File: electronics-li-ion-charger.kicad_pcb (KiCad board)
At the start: 2 copper layers, 19.1 x 25.4 mm, 20 parts, among them J1 Conn_01x01_Male, J2 Conn_01x01_Male, J3 USB_B_Micro, J4 Conn_01x03_Male, U1 MCP73831-2-OT

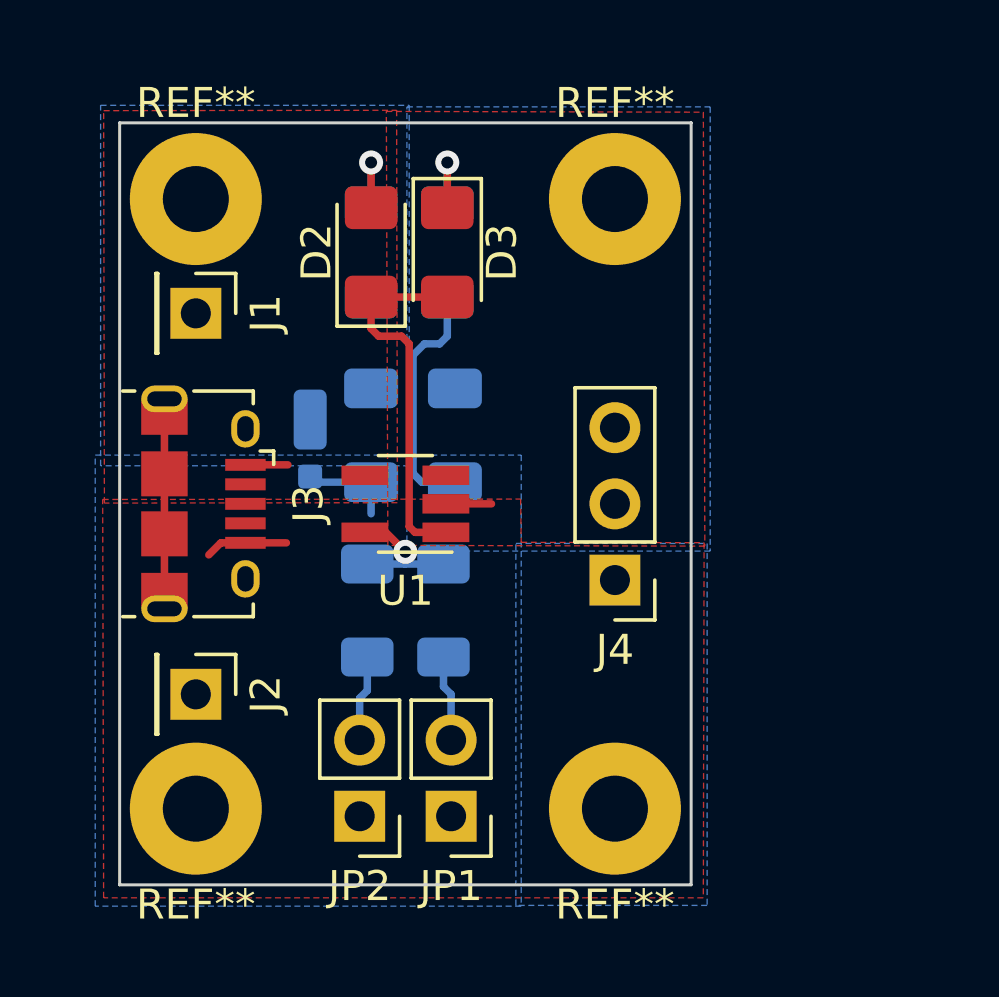
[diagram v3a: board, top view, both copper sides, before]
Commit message: Add silkscreen text.
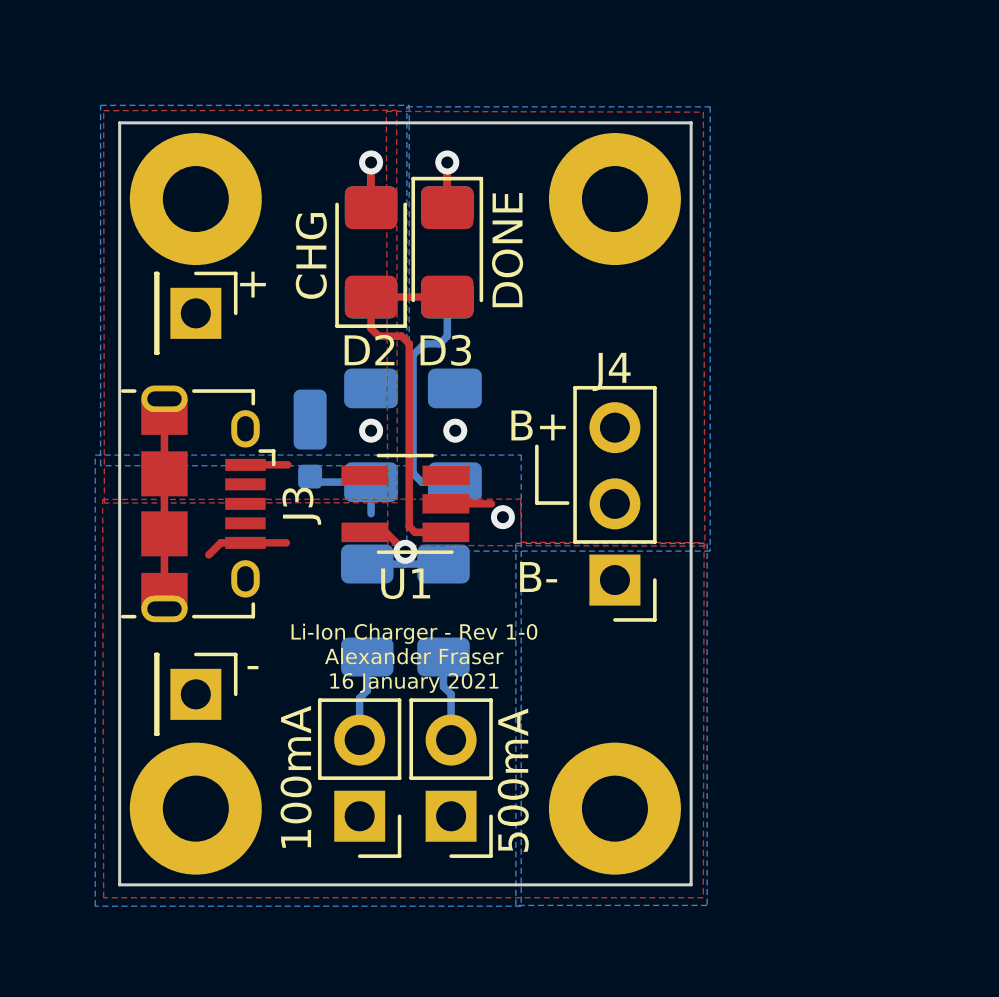
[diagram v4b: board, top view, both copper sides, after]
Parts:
- renumbered REF** to M1, REF** to M2, REF** to M3, REF** to M4
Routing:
- net GND: vias 0 -> 1
- net /VBAT: vias 0 -> 1
- net +5V: vias 0 -> 1
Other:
- board text added: "+"
- board text added: "-"
- board text added: "100mA"
- board text added: "500mA"
- board text added: "B+"
- board text added: "B-"
- board text added: "CHG"
- board text added: "DONE"
- board text added: "Li-Ion Charger - Rev 1-0 Alexander Fraser 16 January 2021"
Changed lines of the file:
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@@
   (general
     (thickness 1.6)
-    (drawings 4)
-    (tracks 45)
+    (drawings 20)
+    (tracks 48)
     (zones 0)
     (modules 20)
@@
     (pad_to_mask_clearance 0)
     (aux_axis_origin 0 0)
-    (visible_elements 7FF9FFFF)
+    (visible_elements 7FFDFFFF)
     (pcbplotparams
       (layerselection 0x010fc_ffffffff)
@@
     (tags "mounting hole 2.2mm m2")
     (attr virtual)
-    (fp_text reference REF** (at 0 -3.2) (layer F.SilkS)
+    (fp_text reference M2 (at 0 -3.2) (layer F.SilkS) hide
       (effects (font (size 1 1) (thickness 0.15)))
     )
@@
     (tags "mounting hole 2.2mm m2")
     (attr virtual)
-    (fp_text reference REF** (at 0 -3.2) (layer F.SilkS)
+    (fp_text reference M4 (at 0 -3.2) (layer F.SilkS) hide
       (effects (font (size 1 1) (thickness 0.15)))
     )
@@
     (tags "mounting hole 2.2mm m2")
     (attr virtual)
-    (fp_text reference REF** (at 0 -3.2) (layer F.SilkS)
+    (fp_text reference M3 (at 0 -3.2) (layer F.SilkS) hide
       (effects (font (size 1 1) (thickness 0.15)))
     )
@@
     (tags "mounting hole 2.2mm m2")
     (attr virtual)
-    (fp_text reference REF** (at 0 -3.2) (layer F.SilkS)
+    (fp_text reference M1 (at 0 -3.2) (layer F.SilkS) hide
       (effects (font (size 1 1) (thickness 0.15)))
     )
@@
     (tags "SOT-23-5 hand-soldering")
     (attr smd)
-    (fp_text reference U1 (at 0 -2.9) (layer F.SilkS)
+    (fp_text reference U1 (at -0.0127 -2.6924) (layer F.SilkS)
       (effects (font (size 1 1) (thickness 0.15)))
     )
@@
     (tags "resistor handsolder")
     (attr smd)
-    (fp_text reference R4 (at 0 -1.672 270) (layer B.SilkS)
+    (fp_text reference R4 (at -0.0127 -1.905 270) (layer B.SilkS)
       (effects (font (size 1 1) (thickness 0.15)) (justify mirror))
     )
@@
     (tags "resistor handsolder")
     (attr smd)
-    (fp_text reference R1 (at 0 1.82 270) (layer B.SilkS)
+    (fp_text reference R1 (at -0.0127 -1.8923 270) (layer B.SilkS)
       (effects (font (size 1 1) (thickness 0.15)) (justify mirror))
     )
@@
     (descr "Through hole straight pin header, 1x02, 2.54mm pitch, single row")
     (tags "Through hole pin header THT 1x02 2.54mm single row")
-    (fp_text reference JP2 (at 0 -2.33) (layer F.SilkS)
+    (fp_text reference JP2 (at 0 -2.33) (layer F.SilkS) hide
       (effects (font (size 1 1) (thickness 0.15)))
     )
@@
     (descr "Through hole straight pin header, 1x02, 2.54mm pitch, single row")
     (tags "Through hole pin header THT 1x02 2.54mm single row")
-    (fp_text reference JP1 (at 0 -2.33) (layer F.SilkS)
+    (fp_text reference JP1 (at 0 -2.33) (layer F.SilkS) hide
       (effects (font (size 1 1) (thickness 0.15)))
     )
@@
     (descr "Through hole straight pin header, 1x03, 2.54mm pitch, single row")
     (tags "Through hole pin header THT 1x03 2.54mm single row")
-    (fp_text reference J4 (at 0 -2.33) (layer F.SilkS)
+    (fp_text reference J4 (at 0.0381 7.0358) (layer F.SilkS)
       (effects (font (size 1 1) (thickness 0.15)))
     )
@@
     (tags "USB Micro B horizontal SMD")
     (attr smd)
-    (fp_text reference J3 (at 0 -3.5 90) (layer F.SilkS)
+    (fp_text reference J3 (at -0.0127 -3.1877 90) (layer F.SilkS)
       (effects (font (size 1 1) (thickness 0.15)))
     )
@@
     (descr "Through hole straight pin header, 1x01, 2.54mm pitch, single row")
     (tags "Through hole pin header THT 1x01 2.54mm single row")
-    (fp_text reference J2 (at 0 -2.33 90) (layer F.SilkS)
+    (fp_text reference J2 (at 0 -2.33 90) (layer F.SilkS) hide
       (effects (font (size 1 1) (thickness 0.15)))
     )
@@
     (descr "Through hole straight pin header, 1x01, 2.54mm pitch, single row")
     (tags "Through hole pin header THT 1x01 2.54mm single row")
-    (fp_text reference J1 (at 0 -2.33 90) (layer F.SilkS)
+    (fp_text reference J1 (at 0 -2.33 90) (layer F.SilkS) hide
       (effects (font (size 1 1) (thickness 0.15)))
     )
@@
     (tags "LED handsolder")
     (attr smd)
-    (fp_text reference D3 (at 0 -1.82 90) (layer F.SilkS)
+    (fp_text reference D3 (at 3.302 0.0635 180) (layer F.SilkS)
       (effects (font (size 1 1) (thickness 0.15)))
     )
@@
     (tags "LED handsolder")
     (attr smd)
-    (fp_text reference D2 (at 0 -1.82 90) (layer F.SilkS)
+    (fp_text reference D2 (at -3.302 -0.0508 180) (layer F.SilkS)
       (effects (font (size 1 1) (thickness 0.15)))
     )
@@
     (tags diode)
     (attr smd)
-    (fp_text reference D1 (at 0 1.5 270) (layer B.SilkS)
+    (fp_text reference D1 (at 1.8161 1.4097 270) (layer B.SilkS)
       (effects (font (size 1 1) (thickness 0.15)) (justify mirror))
     )
@@
     (tags "capacitor handsolder")
     (attr smd)
-    (fp_text reference C2 (at 0 1.85 270) (layer B.SilkS)
+    (fp_text reference C2 (at 0 -1.9304 270) (layer B.SilkS)
       (effects (font (size 1 1) (thickness 0.15)) (justify mirror))
     )
@@
     (tags "capacitor handsolder")
     (attr smd)
-    (fp_text reference C1 (at 0 1.85 270) (layer B.SilkS)
+    (fp_text reference C1 (at -2.9845 1.7907 270) (layer B.SilkS)
       (effects (font (size 1 1) (thickness 0.15)) (justify mirror))
     )
@@
     )
   )
+  (gr_text "Li-Ion Charger - Rev 1-0\nAlexander Fraser\n16 January 2021" (at 136.8171 106.7054) (layer F.SilkS)
+    (effects (font (size 0.508 0.508) (thickness 0.127)))
+  )
+  (gr_text - (at 141.8971 104.0765) (layer B.SilkS)
+    (effects (font (size 1 1) (thickness 0.15)) (justify mirror))
+  )
+  (gr_text + (at 141.8971 101.5746) (layer B.SilkS)
+    (effects (font (size 1 1) (thickness 0.15)) (justify mirror))
+  )
+  (gr_text + (at 141.9352 99.0219) (layer B.SilkS)
+    (effects (font (size 1 1) (thickness 0.15)) (justify mirror))
+  )
+  (gr_line (start 140.9065 101.5746) (end 140.9065 99.6823) (layer F.SilkS) (width 0.12))
+  (gr_line (start 141.9352 101.5746) (end 140.9065 101.5746) (layer F.SilkS) (width 0.12))
+  (gr_text B+ (at 140.97 99.0219) (layer F.SilkS)
+    (effects (font (size 1 1) (thickness 0.15)))
+  )
+  (gr_text B- (at 140.9319 104.0765) (layer F.SilkS)
+    (effects (font (size 1 1) (thickness 0.15)))
+  )
+  (gr_text - (at 131.445 106.9721) (layer F.SilkS)
+    (effects (font (size 1 1) (thickness 0.15)))
+  )
+  (gr_text + (at 131.445 94.2594) (layer F.SilkS)
+    (effects (font (size 1 1) (thickness 0.15)))
+  )
+  (gr_text 100mA (at 132.9182 110.7694 90) (layer F.SilkS)
+    (effects (font (size 1 1) (thickness 0.15)))
+  )
+  (gr_text 500mA (at 140.1572 110.8583 90) (layer F.SilkS)
+    (effects (font (size 1 1) (thickness 0.15)))
+  )
+  (gr_text DONE (at 139.9667 93.1672 90) (layer F.SilkS)
+    (effects (font (size 1 1) (thickness 0.15)))
+  )
+  (gr_text CHG (at 133.4262 93.3196 90) (layer F.SilkS)
+    (effects (font (size 1 1) (thickness 0.15)))
+  )
+  (gr_line (start 134.8613 96.2914) (end 135.3439 96.7486) (layer B.SilkS) (width 0.12))
+  (gr_line (start 134.2771 96.2914) (end 134.8613 96.2914) (layer B.SilkS) (width 0.12))
   (gr_line (start 146.05 88.9) (end 146.05 114.3) (layer Edge.Cuts) (width 0.1))
   (gr_line (start 127 88.9) (end 146.05 88.9) (layer Edge.Cuts) (width 0.1))
@@
   (segment (start 130.3736 102.9) (end 129.9718 103.3018) (width 0.25) (layer F.Cu) (net 1))
   (segment (start 131.194 102.9) (end 132.558 102.9) (width 0.25) (layer F.Cu) (net 1))
+  (via (at 139.7762 102.0445) (size 0.8) (drill 0.4) (layers F.Cu B.Cu) (net 1))
   (segment (start 131.194 100.3) (end 132.6088 100.3) (width 0.25) (layer F.Cu) (net 2))
+  (via (at 135.382 99.1616) (size 0.8) (drill 0.4) (layers F.Cu B.Cu) (net 2))
   (segment (start 137.922 94.7055) (end 135.382 94.7055) (width 0.25) (layer F.Cu) (net 3))
   (segment (start 136.845 102.55) (end 137.875 102.55) (width 0.25) (layer F.Cu) (net 3))
@@
   (segment (start 136.5117 103.606) (end 137.795 103.606) (width 0.25) (layer B.Cu) (net 8))
   (segment (start 135.255 103.606) (end 136.5117 103.606) (width 0.25) (layer B.Cu) (net 8))
+  (via (at 138.1887 99.1616) (size 0.8) (drill 0.4) (layers F.Cu B.Cu) (net 9))
   (segment (start 135.382 91.7305) (end 135.382 90.2208) (width 0.25) (layer F.Cu) (net 10))
   (segment (start 135.382 90.2208) (end 135.382 91.668) (width 0.25) (layer B.Cu) (net 10))

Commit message: Run DRC and clean copper planes.
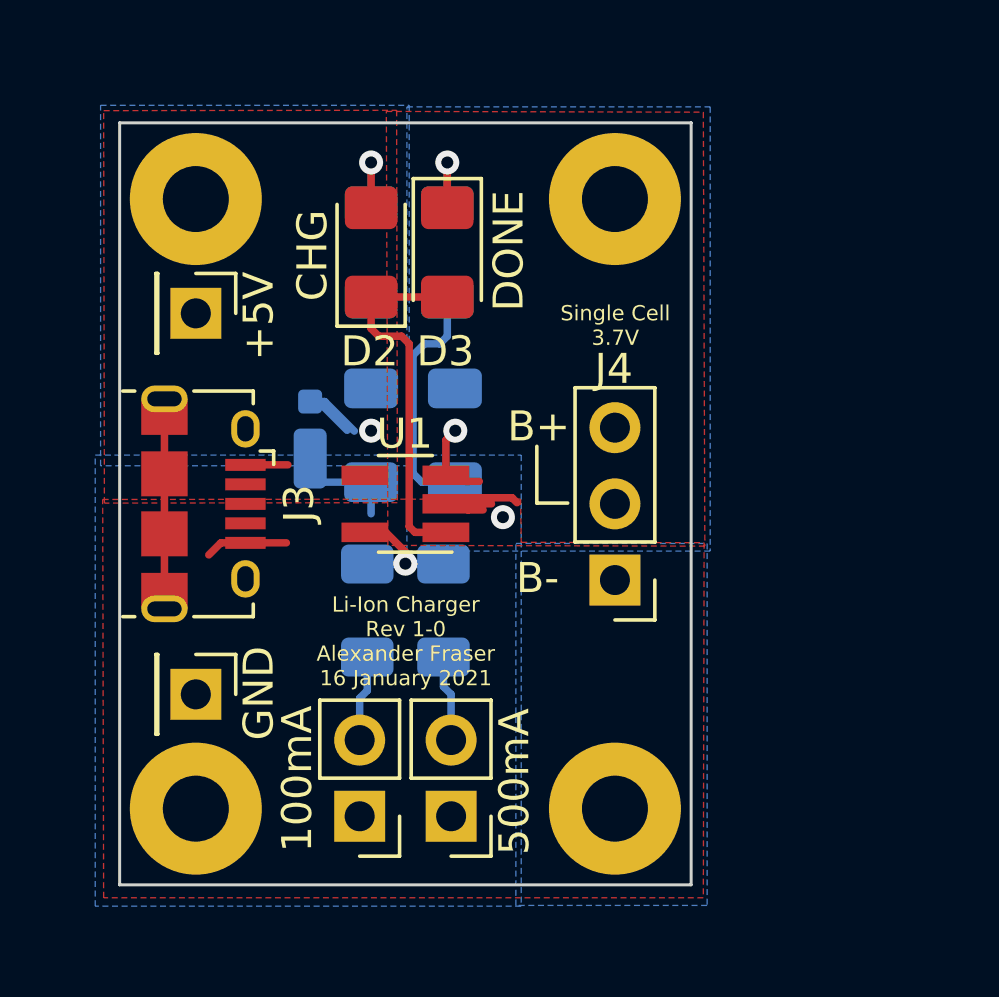
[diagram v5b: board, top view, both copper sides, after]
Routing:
- net GND: track 15.5 -> 20.1 mm
- net +5V: track 1.41 -> 4.92 mm
- net /VBAT: track 0.00 -> 2.82 mm
- net PROG: track 5.34 -> 7.88 mm
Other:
- board text added: "+5V"
- board text added: "GND"
- board text added: "Li-Ion Charger Rev 1-0 Alexander Fraser 16 January 2021"
- board text added: "Single Cell 3.7V"
- board text removed: "Li-Ion Charger - Rev 1-0 Alexander Fraser 16 January 2021"
